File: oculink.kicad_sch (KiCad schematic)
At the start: 17 parts, among them J4 OCuLink_x4_Amphenol_G14A42121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, U10 ESD204DQAR, U11 ESD204DQAR, U8 ESD204DQAR, U9 ESD204DQAR

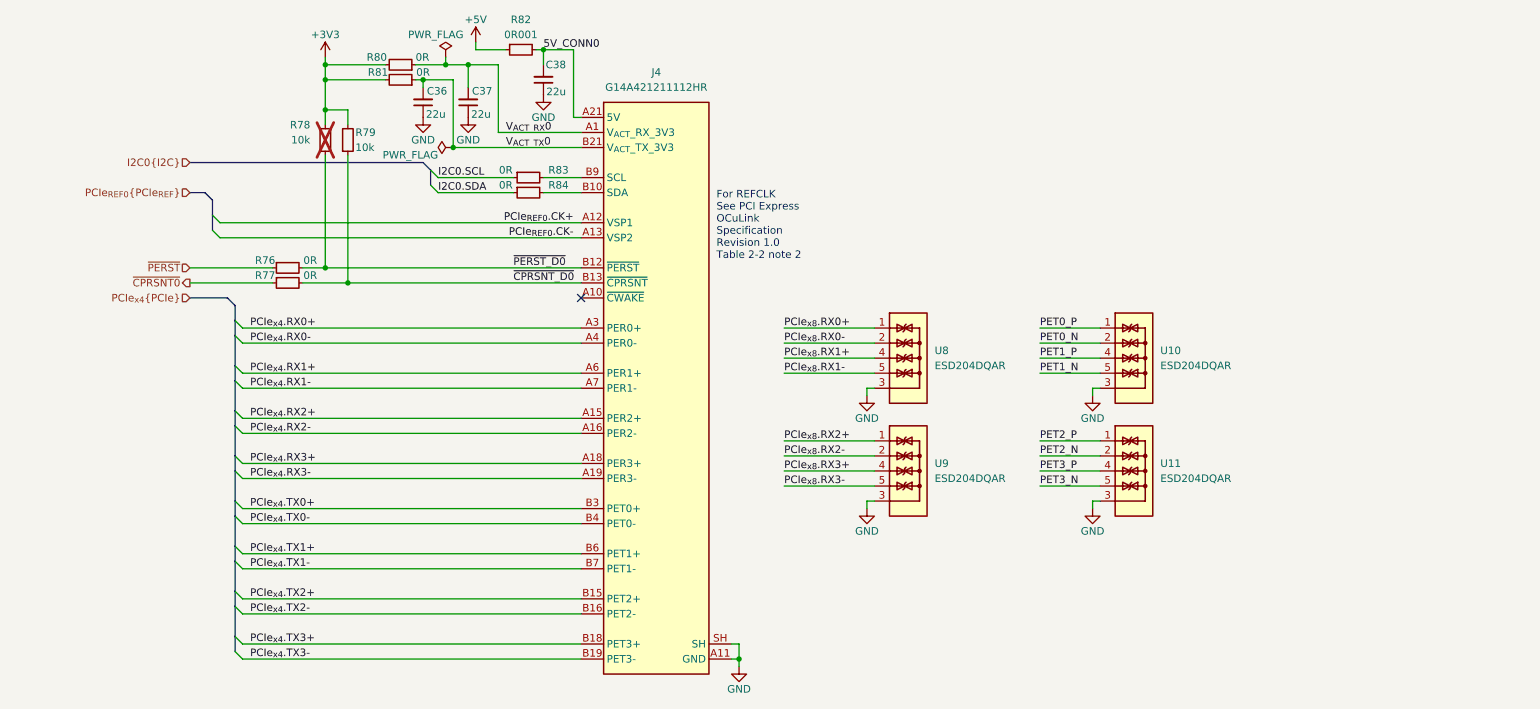
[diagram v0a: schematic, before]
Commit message: [#65447] Layout PCIe, fix net names
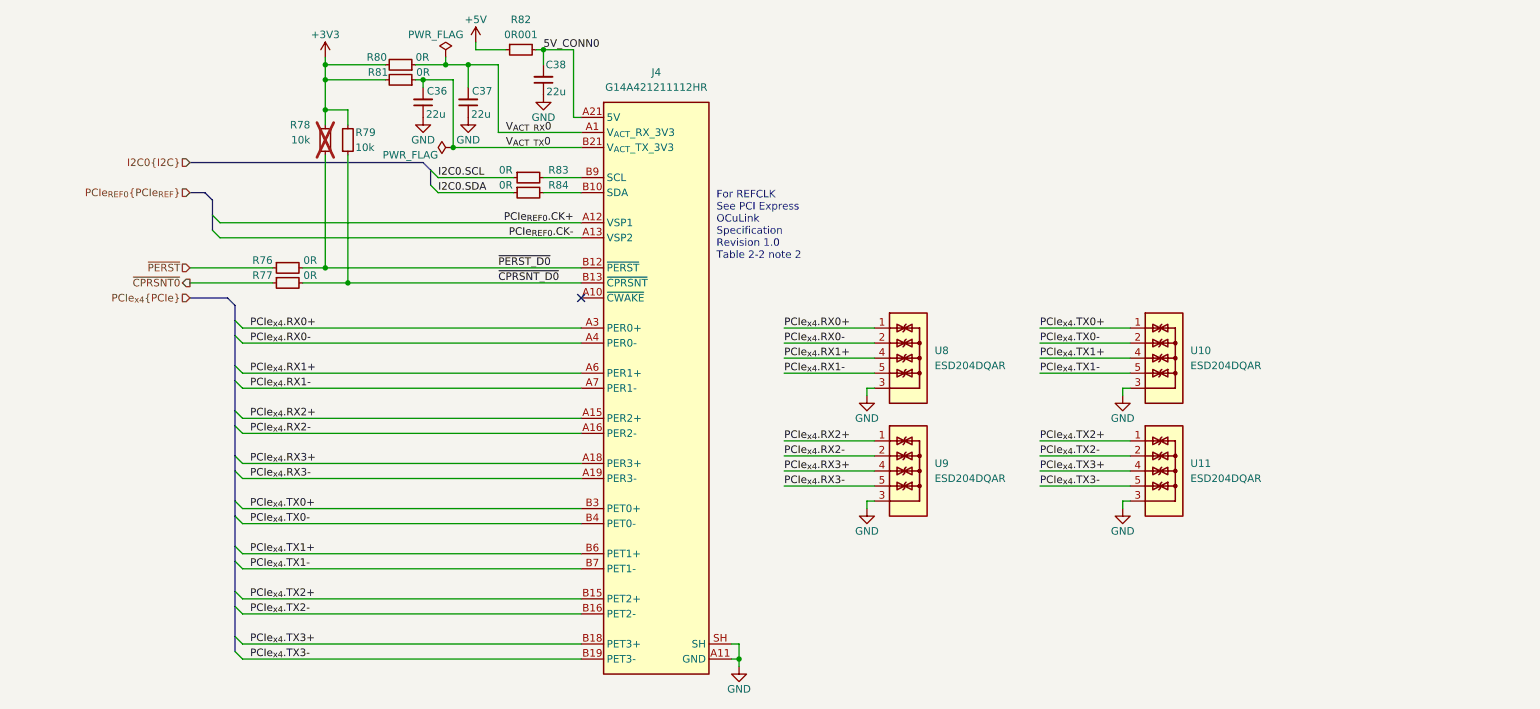
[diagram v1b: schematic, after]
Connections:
- net PCIe_{x8}.RX0+ is gone; now on net PCIe_{x4}.RX0+: U8.1, U8.10
- net PCIe_{x8}.RX0- is gone; now on net PCIe_{x4}.RX0-: U8.2, U8.9
- net PCIe_{x8}.RX1+ is gone; now on net PCIe_{x4}.RX1+: U8.4, U8.7
- net PCIe_{x8}.RX1- is gone; now on net PCIe_{x4}.RX1-: U8.5, U8.6
- net PCIe_{x8}.RX2+ is gone; now on net PCIe_{x4}.RX2+: U9.1, U9.10
- net PCIe_{x8}.RX2- is gone; now on net PCIe_{x4}.RX2-: U9.2, U9.9
- net PCIe_{x8}.RX3+ is gone; now on net PCIe_{x4}.RX3+: U9.4, U9.7
- net PCIe_{x8}.RX3- is gone; now on net PCIe_{x4}.RX3-: U9.5, U9.6
- net PET0_N is gone; now on net PCIe_{x4}.TX0-: U10.2, U10.9
- net PET0_P is gone; now on net PCIe_{x4}.TX0+: U10.1, U10.10
- net PET1_N is gone; now on net PCIe_{x4}.TX1-: U10.5, U10.6
- net PET1_P is gone; now on net PCIe_{x4}.TX1+: U10.4, U10.7
- net PET2_N is gone; now on net PCIe_{x4}.TX2-: U11.2, U11.9
- net PET2_P is gone; now on net PCIe_{x4}.TX2+: U11.1, U11.10
- net PET3_N is gone; now on net PCIe_{x4}.TX3-: U11.5, U11.6
- net PET3_P is gone; now on net PCIe_{x4}.TX3+: U11.4, U11.7
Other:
- moved on the sheet: U10, U11

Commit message: [#67758] Mark CE7 mod. DNP; Add more TVS to J4
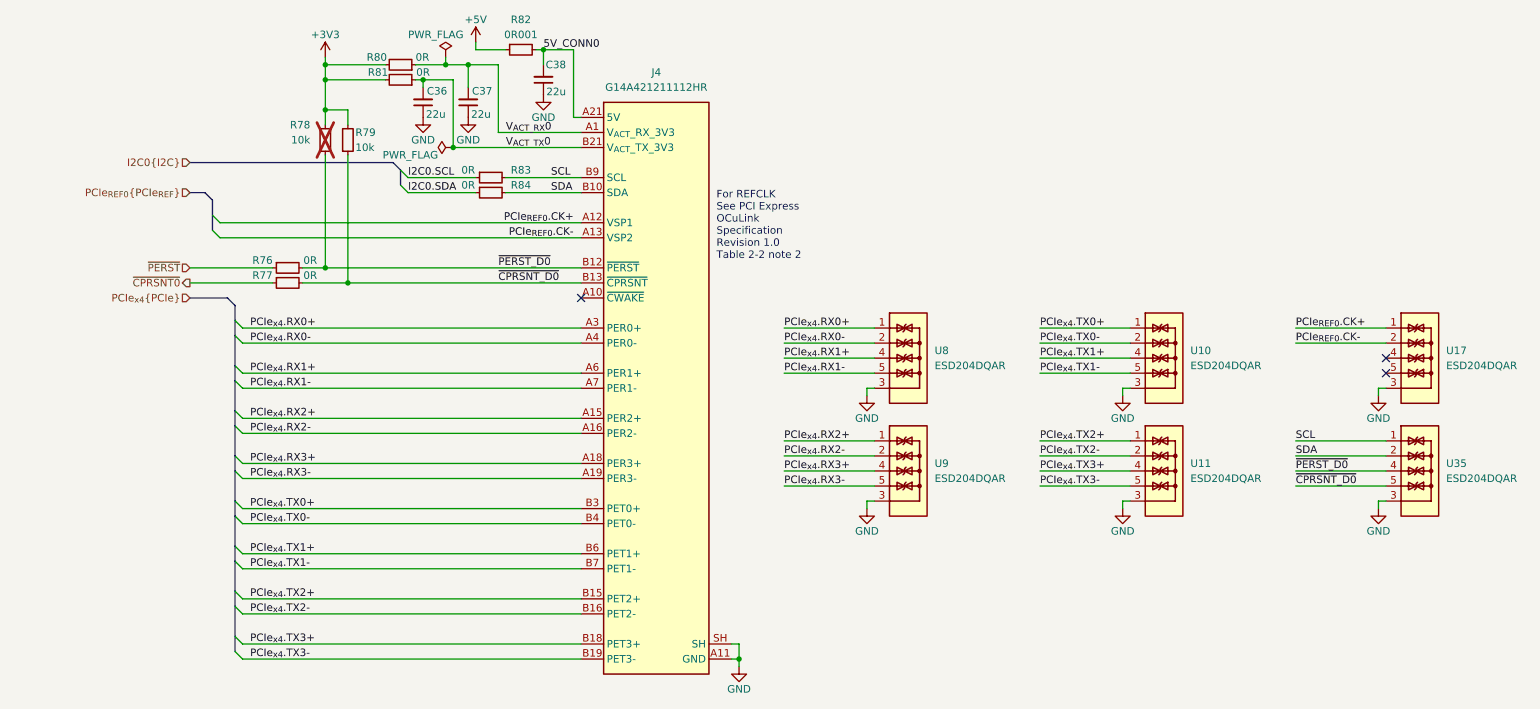
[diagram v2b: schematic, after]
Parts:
- added U17, U35: ESD204DQAR, antmicro-footprints:USON-10_2.5x1mm_P0.5mm, symbol antmicroTVSDiodes:ESD204DQAR
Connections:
- net GND: now also U17.3, U17.8, U35.3, U35.8
- net PCIe_{REF0}.CK+: now also U17.1, U17.10
- net PCIe_{REF0}.CK-: now also U17.2, U17.9
- net ~{CPRSNT_D0}: now also U35.5, U35.6
- net ~{PERST_D0}: now also U35.4, U35.7
- net SDA: now reaches J4.B10 (SDA), R84.2
- net SDA: now also U35.2, U35.9
- net SCL: now reaches J4.B9 (SCL), R83.2
- net SCL: now also U35.1, U35.10
- new net: U17.4, U17.7
- new net: U17.5, U17.6
- no-connect marks 1 -> 3
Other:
- moved on the sheet: R83, R84
